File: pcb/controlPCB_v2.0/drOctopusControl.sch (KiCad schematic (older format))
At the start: 99 parts, among them CON1 PowerPCB2, CON10 Therm, CON11 Therm, CON2 Servo, CON3 Servo, CON4 Outputs, CON5 PowerPCB3, CON6 PowerPCB1, CON7 PIN-2x4, CON8 GND, CON9 GND, Q1 Ceramic_3.7x3.1_8Mhz, SW1 Button, SW2 Reset, SW3 Button, T2 IRLML6244TRPBF, T3 IRLML6244TRPBF, T4 IRLML6244TRPBF, U1 STM32F103RBT6, U2 Oled128x64_M, U4 AMS1117-3.3

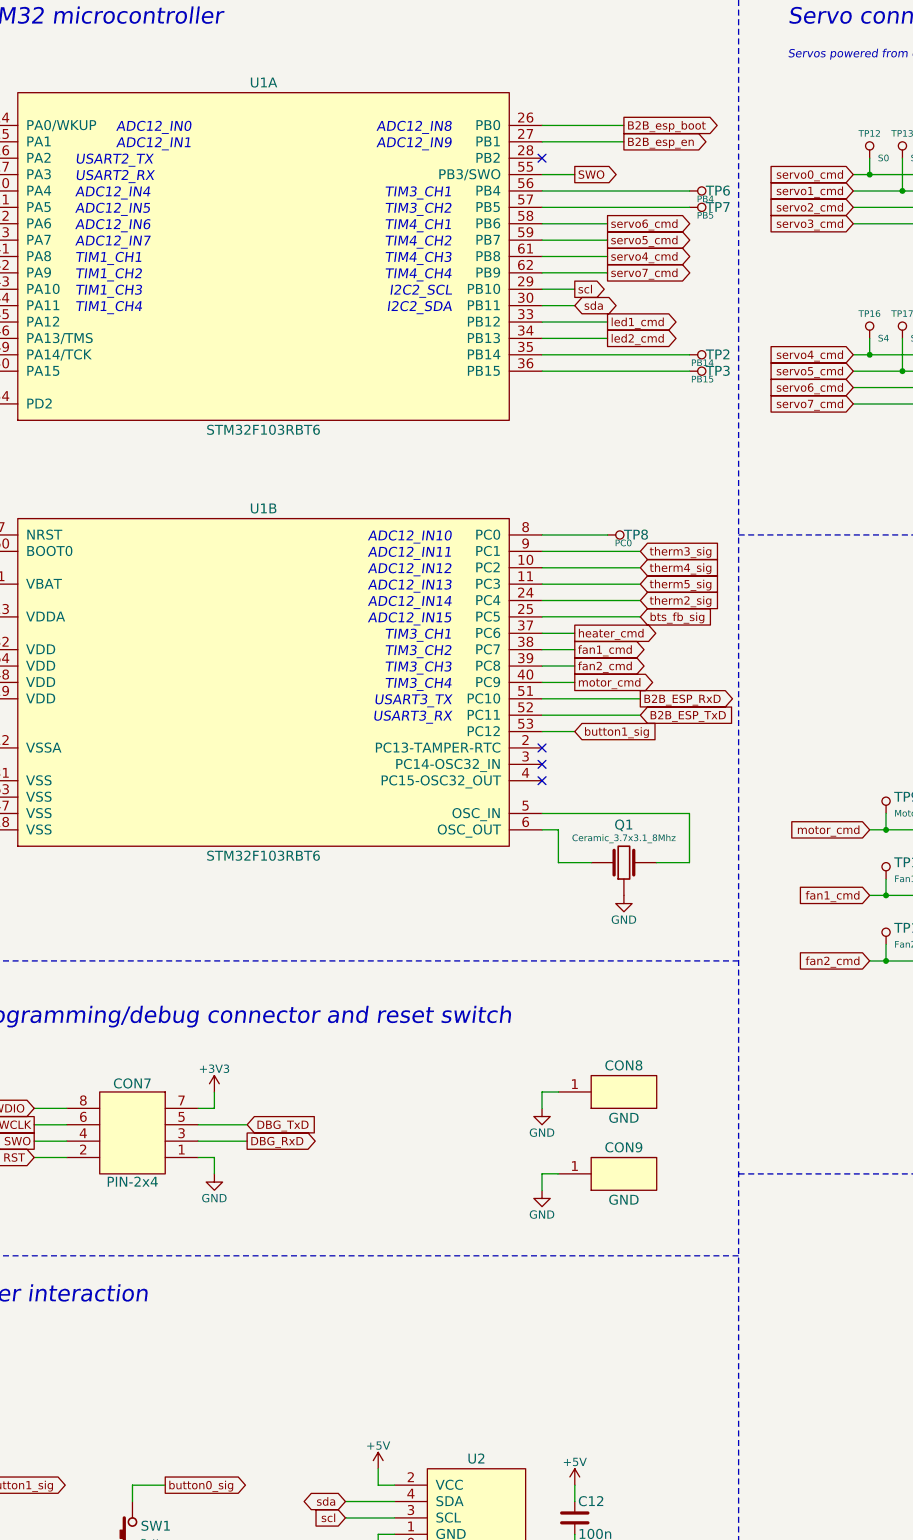
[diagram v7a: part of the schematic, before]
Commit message: Change annotations on schematic.
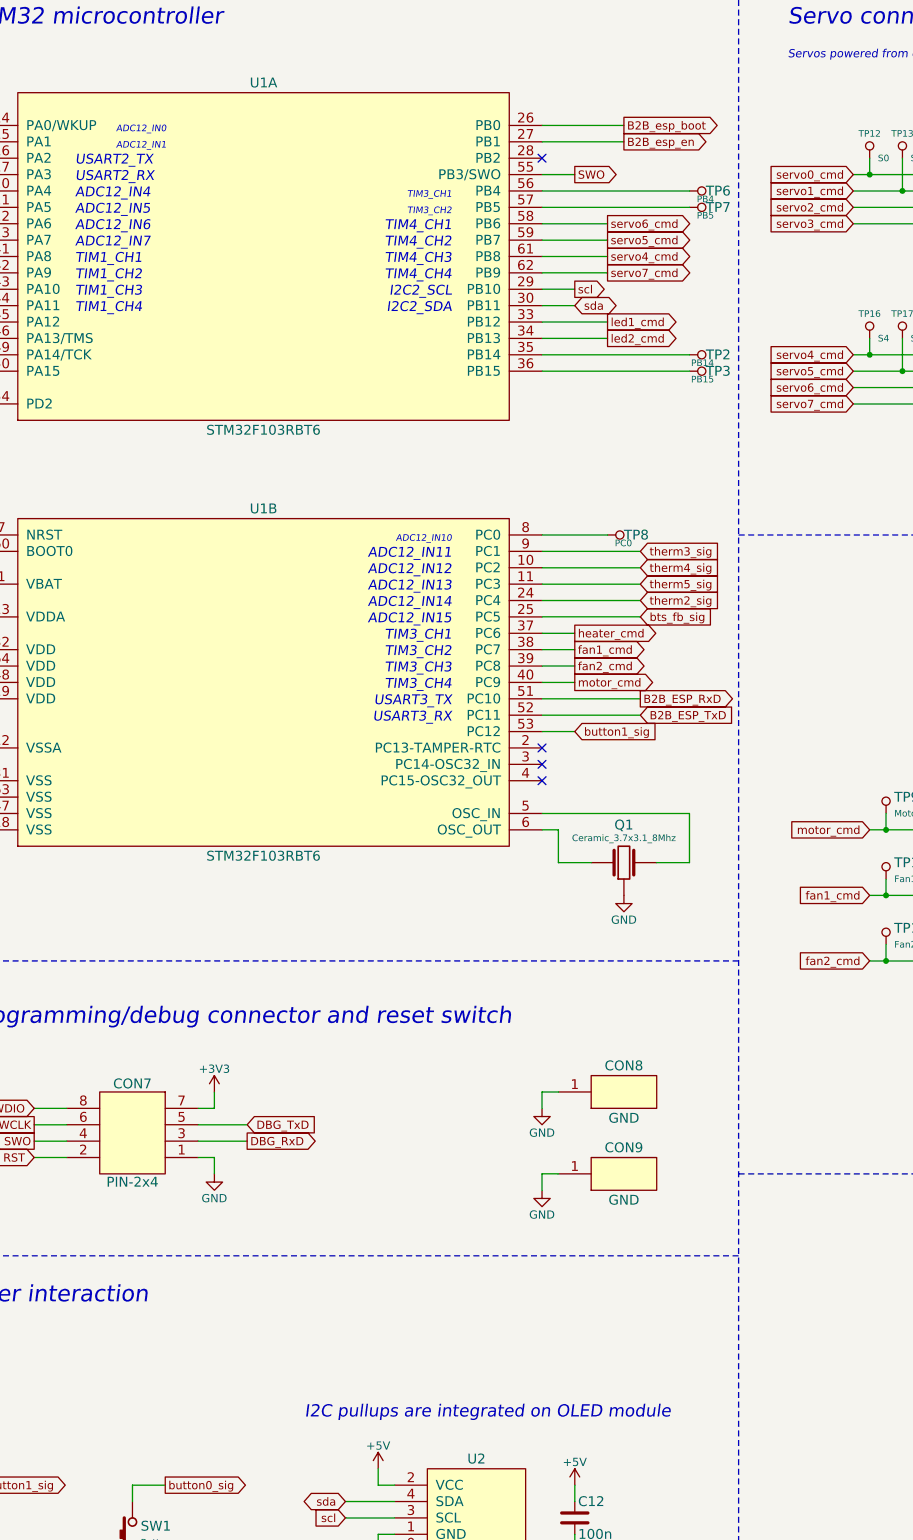
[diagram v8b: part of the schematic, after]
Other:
- note added: "I2C pullups are integrated on OLED module"
- note removed: "ADC12_IN8"
- note removed: "ADC12_IN9"
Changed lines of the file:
@@
 Text Notes 6950 2250 0    60   Italic 0
 ADC12_IN7
-Text Notes 9250 1550 2    60   Italic 0
-ADC12_IN8
-Text Notes 9250 1650 2    60   Italic 0
-ADC12_IN9
 Text Notes 9250 4450 2    60   Italic 0
 ADC12_IN14
 Text Notes 9250 4550 2    60   Italic 0
 ADC12_IN15
-Text Notes 9250 4050 2    60   Italic 0
+Text Notes 9250 4050 2    40   Italic 0
 ADC12_IN10
 Text Notes 9250 4150 2    60   Italic 0
@@
 	1    0    0    -1
 $EndComp
-Text Notes 7200 1550 0    60   Italic 0
-ADC12_IN0
-Text Notes 7200 1650 0    60   Italic 0
-ADC12_IN1
 Text Label 2200 6100 0    50   Italic 0
 B2B_heater_cmd
@@
 	0    1    -1   0
 $EndComp
-Text Notes 9250 1950 2    60   Italic 0
-TIM3_CH1
-Text Notes 9250 2050 2    60   Italic 0
+Text Notes 9250 2050 2    40   Italic 0
 TIM3_CH2
 $Comp
@@
 	1    0    0    -1
 $EndComp
+Text Notes 8350 9400 0    75   Italic 0
+I2C pullups are integrated on OLED module
+Text Notes 9250 1950 2    40   Italic 0
+TIM3_CH1
+Text Notes 7200 1650 0    40   Italic 0
+ADC12_IN1
+Text Notes 7200 1550 0    40   Italic 0
+ADC12_IN0
 $EndSCHEMATC
